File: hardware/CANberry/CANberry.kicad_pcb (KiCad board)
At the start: 2 copper layers, 59 x 28 mm, 85 parts, among them J1 USB_C_Receptacle_USB2.0, J2 0393570003, J3 M20-9990346, J4 SWD, SW1 KMR2, U1 AP2112K-3.3, U2 USBLC6-2SC6, U3 ADM3053, U4 STM32F072C8Tx

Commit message: rename to CANberry due to name colision
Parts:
- added LOGO1: Logo_Open_Hardware_Small, josh-logos:OSHW_Logo_3.6x3.6_F.Mask, F.Cu at (83.5, 45.5)
- C1, C2, C3, C8: value 1u -> 4u7
- D1: value LED -> RED
- D2: value LED -> GRN
- J2: value 0393570003 -> 1751251
- moved svg2mod 0.41 mm to (81.8, 43.5)
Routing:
- net /BOOT0: track 14.8 -> 14.1 mm
- net /nRST: track 23.6 -> 24.2 mm
- net GND: track 45.5 -> 45.4 mm, vias 21 -> 38
- added copper zone on F.Cu, net GND

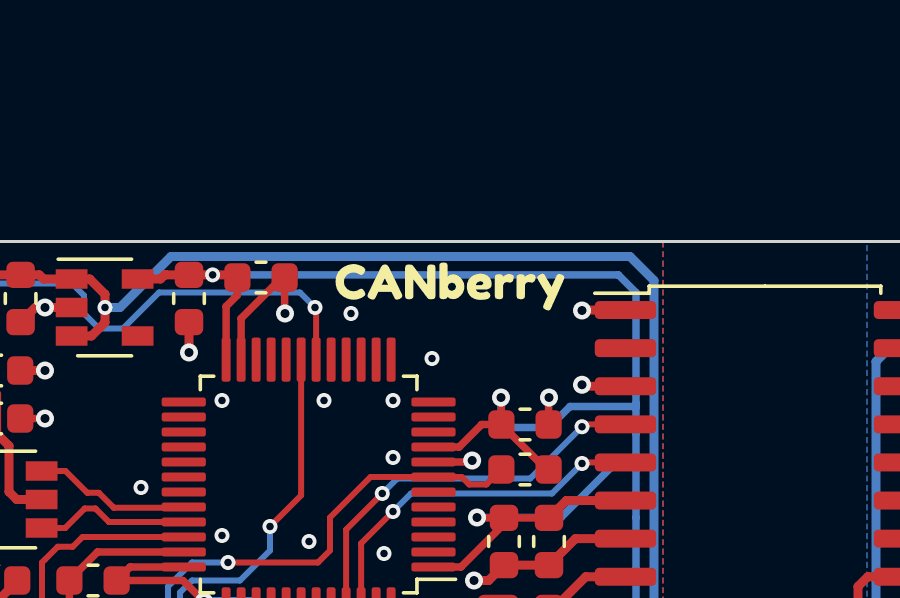
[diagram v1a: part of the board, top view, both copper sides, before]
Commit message: tidy up canberry, add obd/db9 breakout
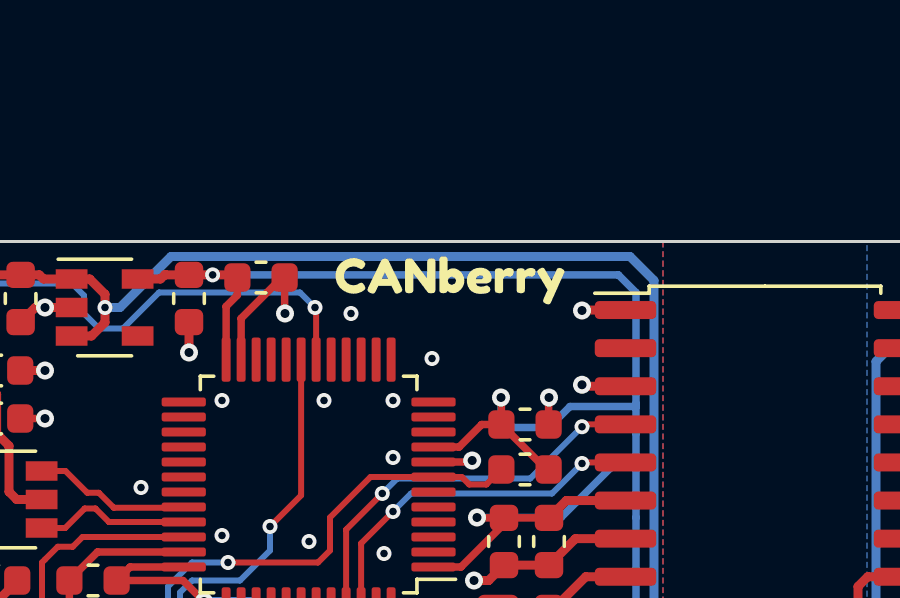
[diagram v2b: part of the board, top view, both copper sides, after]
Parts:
- moved svg2mod 0.20 mm to (81.8, 43.3)
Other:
- board text added: "3V3"
- board text added: "CLK"
- board text added: "GND"
- board text added: "IO"
- board text added: "nRST"
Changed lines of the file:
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@@
     (pad "3" thru_hole oval (at 0.127 5.08 270) (size 1.7 1.7) (drill 1) (layers *.Cu *.Mask)
       (net 63 "Net-(J3-Pad3)") (pinfunction "Pin_3") (pintype "passive"))
+    (model "${KICAD6_3DMODEL_DIR}/Connector_PinHeader_2.54mm.3dshapes/PinHeader_1x03_P2.54mm_Vertical.step"
+      (offset (xyz 0 0 0))
+      (scale (xyz 1 1 1))
+      (rotate (xyz 0 0 0))
+    )
   )
   (footprint "MountingHole:MountingHole_3.2mm_M3" (layer "F.Cu")
@@
   )
   (footprint "svg2mod" (layer "F.Cu")
-    (at 81.8 43.5)
+    (at 81.8 43.3)
     (descr "Converted using: scripting")
     (tags "svg2mod")
@@
       (effects (font (size 1 1) (thickness 0.15)))
     )
+    (fp_line (start 4.775 -1.069) (end 4.646 -0.941) (layer "F.SilkS") (width 0.12))
     (fp_line (start 6.025 1.181) (end 5.931 1.274) (layer "F.SilkS") (width 0.12))
-    (fp_line (start 2.355 0.941) (end 2.226 1.069) (layer "F.SilkS") (width 0.12))
-    (fp_line (start 2.525 1.181) (end 2.431 1.274) (layer "F.SilkS") (width 0.12))
-    (fp_line (start -1.81 -3.16) (end 8.81 -3.16) (layer "F.SilkS") (width 0.12))
-    (fp_line (start -2.05 4.16) (end -2.05 4.8) (layer "F.SilkS") (width 0.12))
-    (fp_line (start -1.81 -3.16) (end -1.81 4.56) (layer "F.SilkS") (width 0.12))
-    (fp_line (start 8.07 -1.275) (end 7.976 -1.181) (layer "F.SilkS") (width 0.12))
-    (fp_line (start -1.81 3) (end 8.81 3) (layer "F.SilkS") (width 0.12))
-    (fp_line (start -1.81 4.56) (end 8.81 4.56) (layer "F.SilkS") (width 0.12))
     (fp_line (start -1.81 4.1) (end 8.81 4.1) (layer "F.SilkS") (width 0.12))
     (fp_line (start 5.855 0.941) (end 5.726 1.069) (layer "F.SilkS") (width 0.12))
-    (fp_line (start 4.775 -1.069) (end 4.646 -0.941) (layer "F.SilkS") (width 0.12))
-    (fp_line (start -2.05 4.8) (end -1.65 4.8) (layer "F.SilkS") (width 0.12))
-    (fp_line (start 8.81 -3.16) (end 8.81 4.56) (layer "F.SilkS") (width 0.12))
     (fp_line (start 4.57 -1.275) (end 4.476 -1.181) (layer "F.SilkS") (width 0.12))
+    (fp_line (start -1.81 4.56) (end 8.81 4.56) (layer "F.SilkS") (width 0.12))
+    (fp_line (start -2.05 4.16) (end -2.05 4.8) (layer "F.SilkS") (width 0.12))
+    (fp_line (start -2.05 4.8) (end -1.65 4.8) (layer "F.SilkS") (width 0.12))
+    (fp_line (start 2.525 1.181) (end 2.431 1.274) (layer "F.SilkS") (width 0.12))
     (fp_line (start 8.275 -1.069) (end 8.146 -0.941) (layer "F.SilkS") (width 0.12))
+    (fp_line (start 2.355 0.941) (end 2.226 1.069) (layer "F.SilkS") (width 0.12))
+    (fp_line (start 8.07 -1.275) (end 7.976 -1.181) (layer "F.SilkS") (width 0.12))
+    (fp_line (start 8.81 -3.16) (end 8.81 4.56) (layer "F.SilkS") (width 0.12))
+    (fp_line (start -1.81 3) (end 8.81 3) (layer "F.SilkS") (width 0.12))
+    (fp_line (start -1.81 -3.16) (end -1.81 4.56) (layer "F.SilkS") (width 0.12))
+    (fp_line (start -1.81 -3.16) (end 8.81 -3.16) (layer "F.SilkS") (width 0.12))
     (fp_arc (start 0 0) (end 1.425 0.891) (angle -64) (layer "F.SilkS") (width 0.12))
     (fp_arc (start 0 0) (end 0.866 -1.44) (angle -63) (layer "F.SilkS") (width 0.12))
-    (fp_arc (start 0 0) (end -0.866 1.44) (angle -32) (layer "F.SilkS") (width 0.12))
-    (fp_arc (start 0 0) (end 0 1.68) (angle -32) (layer "F.SilkS") (width 0.12))
     (fp_arc (start 0 0) (end -1.44 -0.866) (angle -63) (layer "F.SilkS") (width 0.12))
-    (fp_circle (center 3.5 0) (end 5.18 0) (layer "F.SilkS") (width 0.12) (fill none))
+    (fp_arc (start 0 0) (end 0 1.68) (angle -32) (layer "F.SilkS") (width 0.12))
+    (fp_arc (start 0 0) (end -0.866 1.44) (angle -32) (layer "F.SilkS") (width 0.12))
     (fp_circle (center 7 0) (end 8.68 0) (layer "F.SilkS") (width 0.12) (fill none))
+    (fp_circle (center 3.5 0) (end 5.18 0) (layer "F.SilkS") (width 0.12) (fill none))
+    (fp_line (start 9.25 5) (end 9.25 -3.6) (layer "F.CrtYd") (width 0.05))
     (fp_line (start -2.25 -3.6) (end -2.25 5) (layer "F.CrtYd") (width 0.05))
     (fp_line (start -2.25 5) (end 9.25 5) (layer "F.CrtYd") (width 0.05))
     (fp_line (start 9.25 -3.6) (end -2.25 -3.6) (layer "F.CrtYd") (width 0.05))
-    (fp_line (start 9.25 5) (end 9.25 -3.6) (layer "F.CrtYd") (width 0.05))
+    (fp_line (start -1.75 -3.1) (end 8.75 -3.1) (layer "F.Fab") (width 0.1))
     (fp_line (start 4.638 -0.955) (end 2.546 1.138) (layer "F.Fab") (width 0.1))
-    (fp_line (start -1.75 4.1) (end -1.75 -3.1) (layer "F.Fab") (width 0.1))
+    (fp_line (start 0.955 -1.138) (end -1.138 0.955) (layer "F.Fab") (width 0.1))
+    (fp_line (start -1.35 4.5) (end -1.75 4.1) (layer "F.Fab") (width 0.1))
     (fp_line (start -1.75 4.1) (end 8.75 4.1) (layer "F.Fab") (width 0.1))
-    (fp_line (start -1.75 -3.1) (end 8.75 -3.1) (layer "F.Fab") (width 0.1))
+    (fp_line (start -1.75 4.1) (end -1.75 -3.1) (layer "F.Fab") (width 0.1))
     (fp_line (start 1.138 -0.955) (end -0.955 1.138) (layer "F.Fab") (width 0.1))
-    (fp_line (start 7.955 -1.138) (end 5.863 0.955) (layer "F.Fab") (width 0.1))
     (fp_line (start 8.75 4.5) (end -1.35 4.5) (layer "F.Fab") (width 0.1))
+    (fp_line (start 7.955 -1.138) (end 5.863 0.955) (layer "F.Fab") (width 0.1))
+    (fp_line (start 4.455 -1.138) (end 2.363 0.955) (layer "F.Fab") (width 0.1))
     (fp_line (start 8.75 -3.1) (end 8.75 4.5) (layer "F.Fab") (width 0.1))
-    (fp_line (start -1.75 3) (end 8.75 3) (layer "F.Fab") (width 0.1))
-    (fp_line (start -1.35 4.5) (end -1.75 4.1) (layer "F.Fab") (width 0.1))
     (fp_line (start 8.138 -0.955) (end 6.046 1.138) (layer "F.Fab") (width 0.1))
-    (fp_line (start 0.955 -1.138) (end -1.138 0.955) (layer "F.Fab") (width 0.1))
-    (fp_line (start 4.455 -1.138) (end 2.363 0.955) (layer "F.Fab") (width 0.1))
+    (fp_line (start -1.75 3) (end 8.75 3) (layer "F.Fab") (width 0.1))
     (fp_circle (center 0 0) (end 1.5 0) (layer "F.Fab") (width 0.1) (fill none))
-    (fp_circle (center 3.5 0) (end 5 0) (layer "F.Fab") (width 0.1) (fill none))
     (fp_circle (center 7 0) (end 8.5 0) (layer "F.Fab") (width 0.1) (fill none))
+    (fp_circle (center 3.5 0) (end 5 0) (layer "F.Fab") (width 0.1) (fill none))
     (pad "1" thru_hole rect locked (at 0 0 270) (size 2.4 2.4) (drill 1.2) (layers *.Cu *.Mask)
-      (net 11 "/CAN_H") (pinfunction "Pin_1") (pintype "passive"))
+      (net 11 "/CAN_H") (pinfunction "Pin_1"))
     (pad "2" thru_hole circle locked (at 3.5 0 270) (size 2.4 2.4) (drill 1.2) (layers *.Cu *.Mask)
-      (net 12 "/CAN_L") (pinfunction "Pin_2") (pintype "passive"))
+      (net 12 "/CAN_L") (pinfunction "Pin_2"))
     (pad "3" thru_hole circle locked (at 7 0 270) (size 2.4 2.4) (drill 1.2) (layers *.Cu *.Mask)
-      (net 6 "GNDD") (pinfunction "Pin_3") (pintype "passive"))
+      (net 6 "GNDD") (pinfunction "Pin_3"))
+    (model "${KIPRJMOD}/../../josh-kicad-lib/packages3d/josh-connectors/393570003.stp"
+      (offset (xyz 3.5 -0.3 0))
+      (scale (xyz 1 1 1))
+      (rotate (xyz 90 180 -180))
+    )
   )
   (footprint "Capacitor_SMD:C_0603_1608Metric" (layer "F.Cu")
@@
   (gr_line (start 114 39) (end 114 61) (layer "Edge.Cuts") (width 0.1))
   (gr_arc (start 111 39) (end 114 39) (angle -180) (layer "Edge.Cuts") (width 0.1))
+  (gr_text "3V3" (at 77 53.4 90) (layer "B.SilkS")
+    (effects (font (size 1 1) (thickness 0.15)) (justify mirror))
+  )
+  (gr_text "IO" (at 69.4 54.1 90) (layer "B.SilkS")
+    (effects (font (size 1 1) (thickness 0.15)) (justify mirror))
+  )
+  (gr_text "GND" (at 72 53.3 90) (layer "B.SilkS")
+    (effects (font (size 1 1) (thickness 0.15)) (justify mirror))
+  )
+  (gr_text "nRST" (at 66.8 53.1 90) (layer "B.SilkS")
+    (effects (font (size 1 1) (thickness 0.15)) (justify mirror))
+  )
+  (gr_text "CLK" (at 74.5 53.4 90) (layer "B.SilkS")
+    (effects (font (size 1 1) (thickness 0.15)) (justify mirror))
+  )
   (segment (start 61.2 48.74669) (end 61.2 51.45331) (width 0.3) (layer "F.Cu") (net 1))
   (segment (start 67.3575 50.6) (end 67.1 50.3425) (width 0.3) (layer "F.Cu") (net 1))
